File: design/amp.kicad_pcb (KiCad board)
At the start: 2 copper layers, 61 x 36 mm, 48 parts, among them IC1 CP2102N-A02-GQFN24R, IC2 STM6601CQ2BDM6F, IC3 LD39200PU33R, J1 12401610E4#2A, J2 TSW-104-08-T-T-RA, J3 Conn_01x02_Female, J4 Conn_02x03_Odd_Even, Q1 PMBT2222,215, Q2 PMBT2222,215, Q3 Si2347DS-T1-GE3, U1 ESP32-WROOM-32D, U2 LIS2HH12

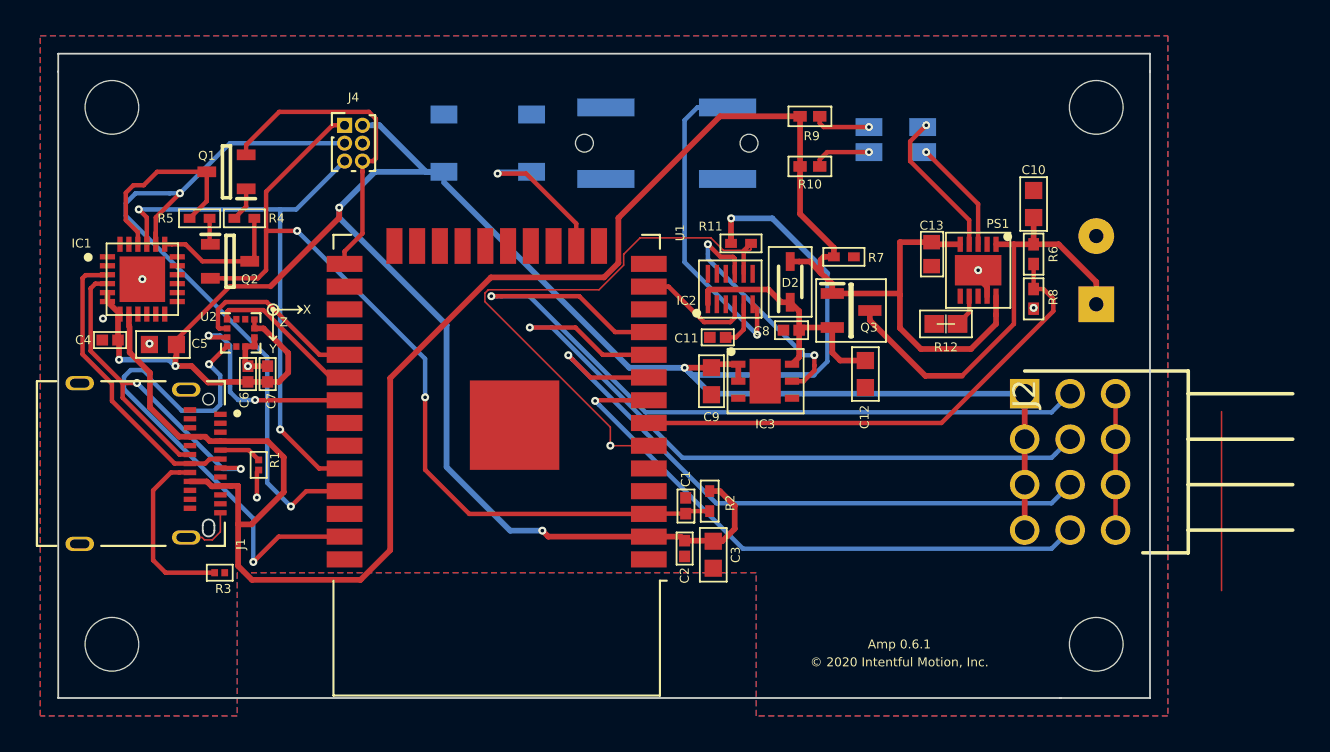
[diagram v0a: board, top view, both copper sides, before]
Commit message: updated to new USB connector. Flipped status led and input button
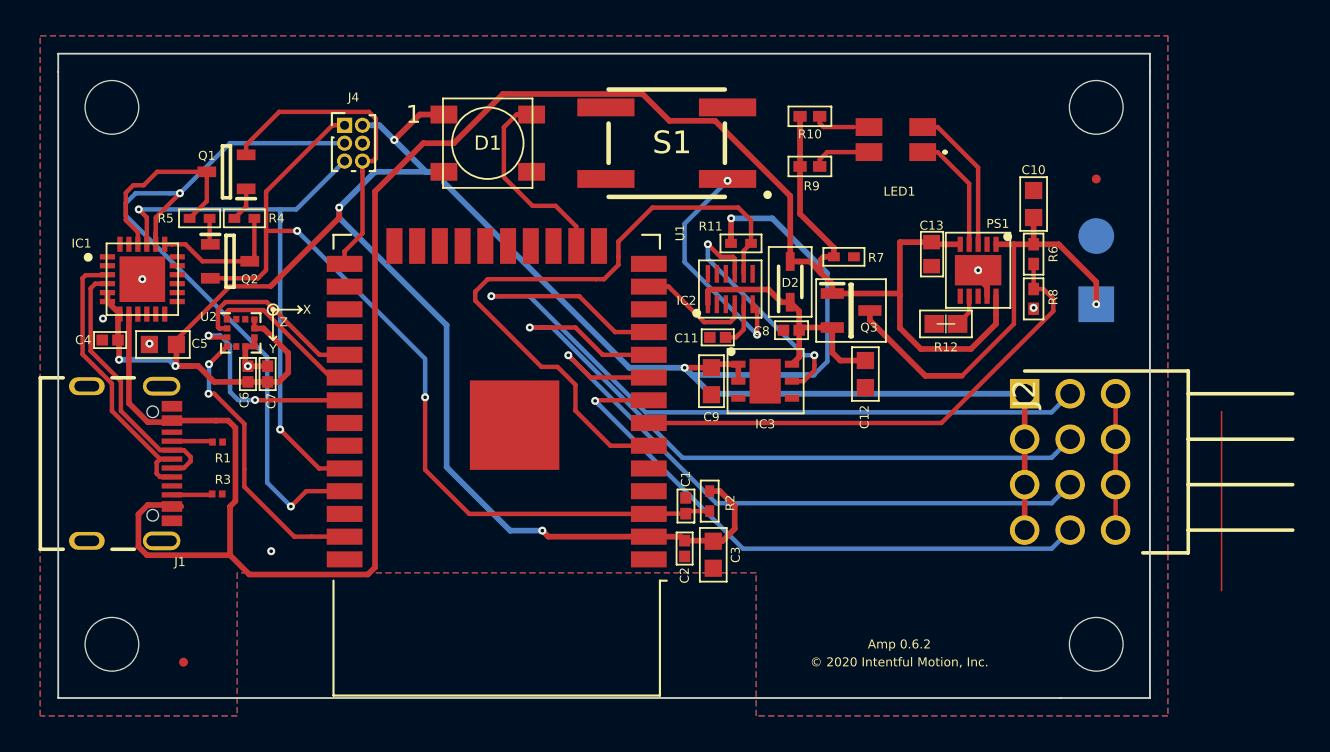
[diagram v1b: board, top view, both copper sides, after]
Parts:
- removed H5, H6: MountingHole, MountingHole:MountingHole_2.2mm_M2_ISO7380
- added FID1: Fiducial, Fiducial:Fiducial_0.5mm_Mask1.5mm, F.Cu at (62.0, 66.0)
- added FID2: Fiducial, Fiducial:Fiducial_0.5mm_Mask1.5mm, F.Cu at (113.0, 39.0)
- D1, LED1, S1: moved to F.Cu
- J1: value 12401610E4#2A -> USB4105-GF-A; footprint 12401610E4_2A:AMPHENOL_12401610E4#2A -> USB4105-GF-A:GCT_USB4105-GF-A
- moved J1 6.80 mm to (56.6, 54.9)
- moved R3 4.40 mm to (63.9, 56.6)
- moved R10 2.80 mm to (97.0, 35.5)
- moved R9 2.80 mm to (97.0, 38.3)
- moved R1 2.63 mm to (63.9, 53.7), turned to 180 degrees
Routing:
- net /MOSI: track 29.7 -> 16.1 mm
- net /VBUS: track 110.0 -> 123.4 mm
- net Net-(J1-PadB5): track 10.1 -> 2.27 mm
- net /D-: track 22.7 -> 15.0 mm, vias 2 -> 0
- net GND: track 17.9 -> 12.6 mm
- net /PB_INPUT: track 18.2 -> 13.1 mm, vias 1 -> 2
- net +3V3: track 154.5 -> 158.7 mm, vias 6 -> 7
- net /AMP_INPUT: track 32.6 -> 36.0 mm, vias 1 -> 0
- net /STATUS_LED: track 8.74 -> 10.9 mm, vias 1 -> 0
- net Net-(LED1-Pad3): track 6.35 -> 8.33 mm, vias 1 -> 0
- net Net-(LED1-Pad1): track 8.66 -> 6.99 mm, vias 1 -> 0
- net /D+: track 16.6 -> 15.9 mm
- net Net-(LED1-Pad4): track 3.31 -> 3.23 mm, vias 1 -> 0
- net Net-(LED1-Pad2): track 3.23 -> 3.31 mm, vias 1 -> 0
- net /VBAT: vias 0 -> 1
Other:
- board text added: "Amp 0.6.2"
- board text removed: "Amp 0.6.1"
